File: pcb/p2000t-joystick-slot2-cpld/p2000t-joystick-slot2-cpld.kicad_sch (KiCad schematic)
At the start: 24 parts, among them J1 PLAYER1, J2 P2000T Port 2, J3 PLAYER2, J4 Atmel-JTAG-10, J5 POWER, SW1 SW_DIP_x02, U3 ATF1502ASV

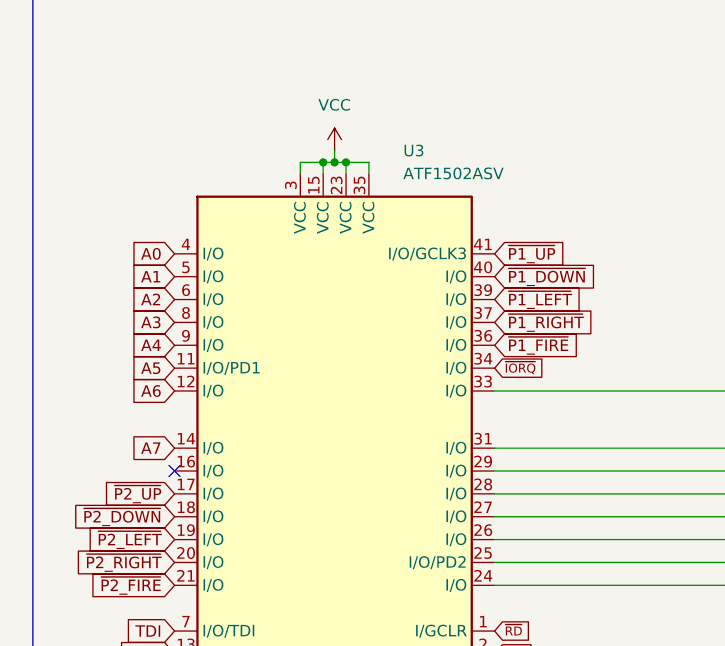
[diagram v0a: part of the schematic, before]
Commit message: Fixing design and CUPL
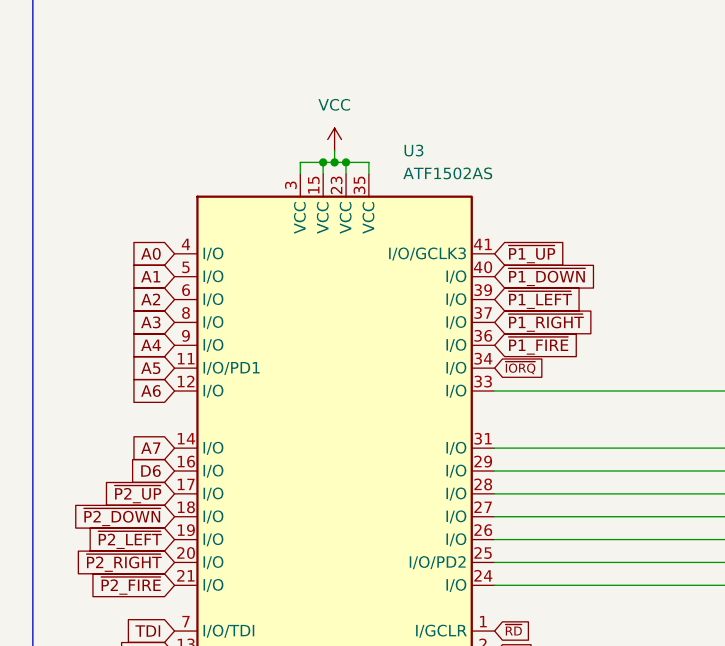
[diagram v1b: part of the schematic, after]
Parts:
- U3: value ATF1502ASV -> ATF1502AS
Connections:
- net D6: now also U3.16 (I/O)
- no-connect marks 10 -> 9
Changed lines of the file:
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@@
 	)
 	(no_connect
-		(at 31.75 66.04)
-	)
-	(no_connect
 		(at 264.16 58.42)
 	)
@@
 		)
 	)
+	(global_label "D6"
+		(shape input)
+		(at 31.75 66.04 180)
+		(fields_autoplaced yes)
+		(effects
+			(font
+				(size 1.27 1.27)
+			)
+			(justify right)
+		)
+		(property "Intersheetrefs" "${INTERSHEET_REFS}"
+			(at 26.2853 66.04 0)
+			(effects
+				(font
+					(size 1.27 1.27)
+				)
+				(justify right)
+				(hide yes)
+			)
+		)
+	)
 	(global_label "~{P1_LEFT}"
 		(shape input)
@@
 			)
 		)
-		(property "Value" "ATF1502ASV"
+		(property "Value" "ATF1502AS"
 			(at 57.15 33.02 0)
 			(effects
